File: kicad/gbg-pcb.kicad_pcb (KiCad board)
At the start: 2 copper layers, 99.1 x 99.1 mm, 74 parts, among them J1 1017514, J2 Screw_Terminal_01x04, J3 Screw_Terminal_01x03, J4 1017514, J5 VP0265840000G, J6 Conn_01x09_Pin, J7 Conn_01x02, Q1 SQD40031EL_GE3, Q2 SQD40031EL_GE3, Q3 SQD40031EL_GE3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

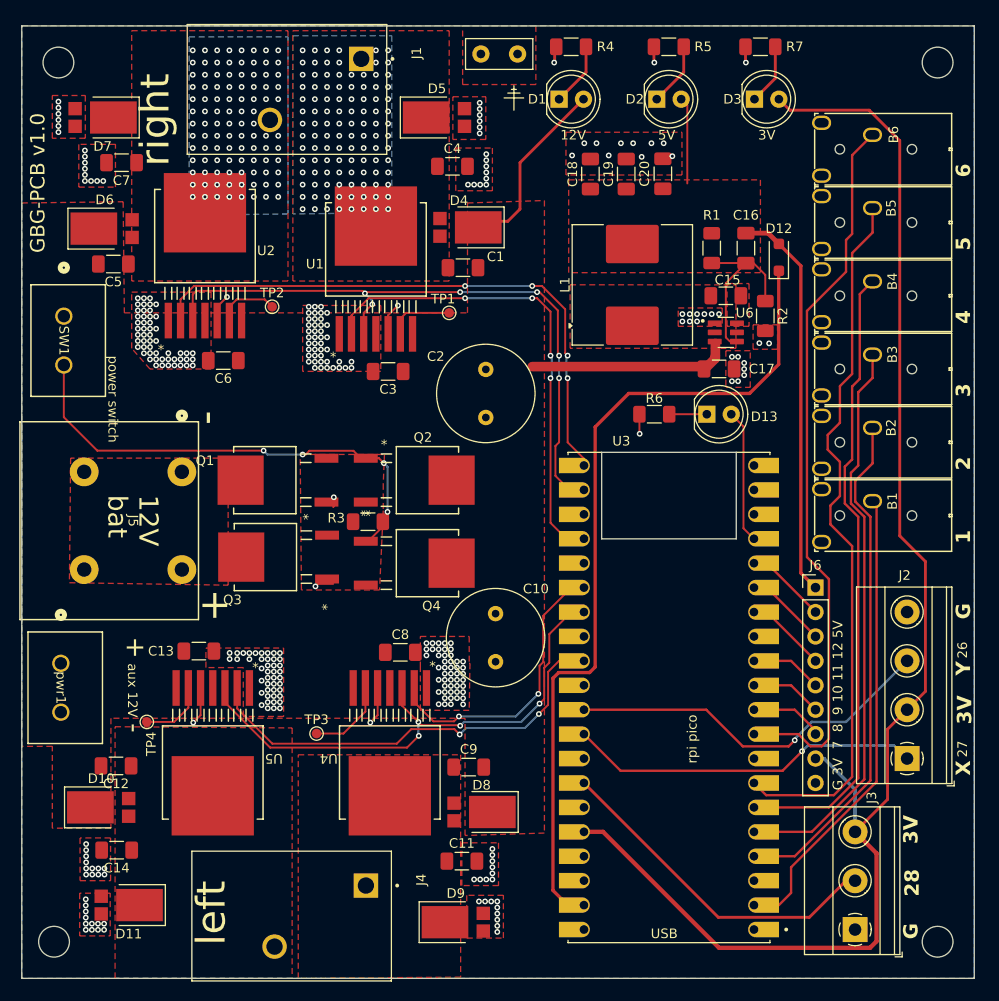
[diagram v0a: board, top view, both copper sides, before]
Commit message: automatically render images
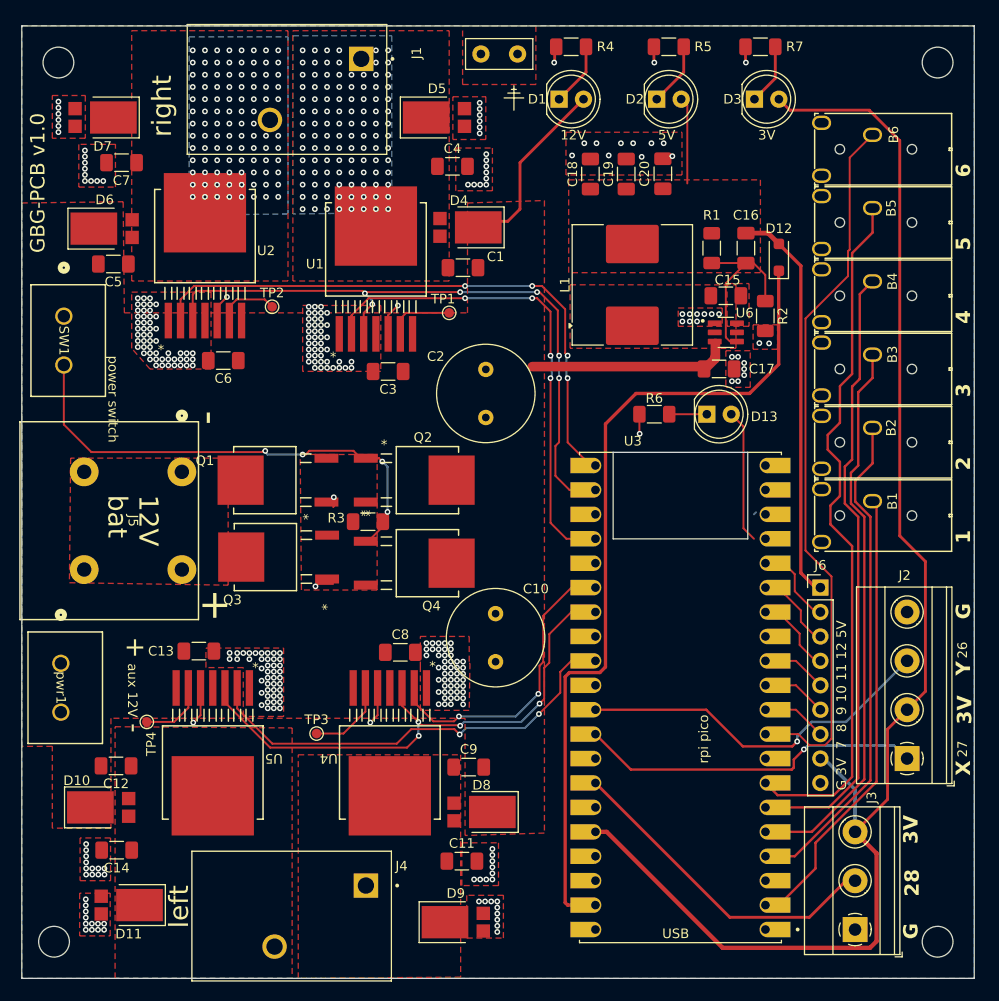
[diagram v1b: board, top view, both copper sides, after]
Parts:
- moved U3 1.19 mm to (108.3, 118.0)
- moved J6 0.51 mm to (122.8, 106.6)
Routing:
- net Net-(D12-K): track 87.3 -> 85.8 mm
- net bt5: track 74.5 -> 73.3 mm
- net +3.3V: track 148.2 -> 147.1 mm
- net left_en: track 55.7 -> 56.9 mm
- net bt4: track 65.5 -> 64.4 mm
- net bt3: track 59.4 -> 58.2 mm
- net bt2: track 53.5 -> 52.3 mm
- net Net-(J3-Pin_2): track 35.6 -> 34.4 mm
- net bt1: track 49.4 -> 48.2 mm
- net Net-(J2-Pin_3): track 38.9 -> 38.0 mm
- net Net-(J6-Pin_7): track 7.68 -> 6.77 mm
- net Net-(J2-Pin_1): track 36.8 -> 36.0 mm
- net bt6: track 75.2 -> 74.5 mm
- net Net-(J6-Pin_6): track 7.45 -> 6.77 mm
- net Net-(J6-Pin_5): track 7.45 -> 6.77 mm
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
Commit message: clean up fil zones
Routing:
- net Net-(D8-A): vias 0 -> 98
- net Net-(D10-A): vias 0 -> 105
- added copper zone on B.Cu, net Net-(D10-A)
- added copper zone on B.Cu, net Net-(D8-A)

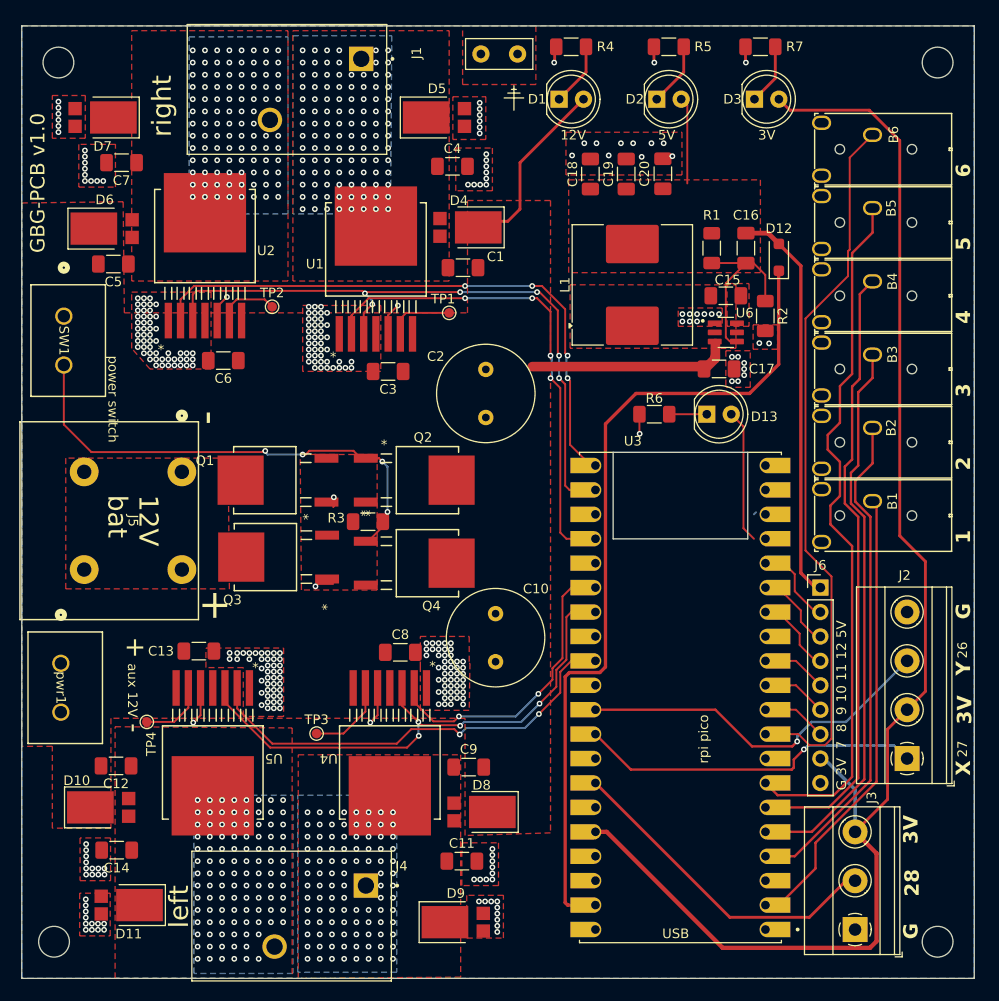
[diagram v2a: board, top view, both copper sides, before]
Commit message: change inductor
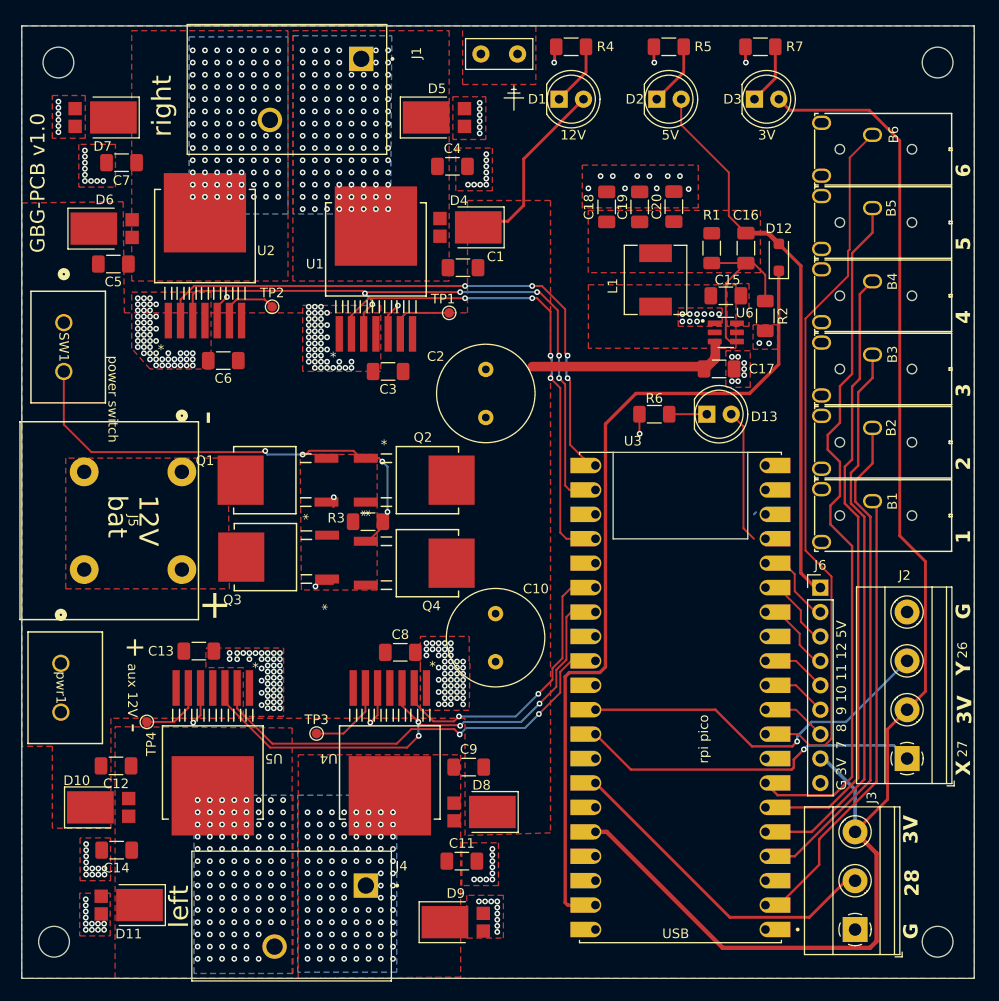
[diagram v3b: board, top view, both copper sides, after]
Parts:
- C15: value 22uF -> 100nF
- C17: value 22uF -> 15uF
- L1: footprint Inductor_SMD:L_Coilcraft_MSS1260T-XXX -> kicad libraries:IND_SRP6540-150M
- moved C18 3.82 mm to (100.6, 67.0)
- moved C19 3.69 mm to (104.0, 67.0)
- moved C20 3.60 mm to (107.6, 66.9)
- moved L1 2.47 mm to (105.7, 74.5)
- moved SW1 0.67 mm to (44.1, 79.0)
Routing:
- net 5V: track 50.2 -> 57.9 mm
- net Net-(U6-SW): track 2.07 -> 0.00 mm
- net Net-(Q2-G): track 51.0 -> 50.3 mm
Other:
- board text added: "sd card? maybe on the back? flyback diodes? could smaller ones be used? think about the +BATT fill - make it thicker? add more capacitors between it and ground? for buck converter, re-do layout. look at datasheet's layout example change motor power screw terminals? think about thermal resistance of parts - how much current can they actually handle? think about how to add heat sinks to this board 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"
- board text removed: "sd card? maybe on the back? flyback diodes? could smaller ones be used? think about the +BATT fill - make it thicker? add more capacitors between it and ground? for buck converter, look at datasheet's layout example change main power screw terminal? it used to be 1017503, consider the same as the motors have 1017514 or terminals with more vertical wire entry 1017514 (screws) or 1017521 (screwless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"

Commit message: move silkscreen
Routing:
- net GND: vias 300 -> 296

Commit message: label pico pins
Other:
- board text added: "15 14 GND 13 led 12 11 10 GND 9 8 7 6 B6 GND 5 B5 4 B4 3 B3 2 B2 GND 1 B1 0"
- board text added: "R2 16 Ren 17 GND R1 18 19 L1 20 Len 21 GND L2 22 RUN Y 26 X 27 GND A2 28 VREF 3.3V EN GND VSYS VBUS"
- board text added: "sd card? maybe on the back? flyback diodes? could smaller ones be used? think about the +BATT fill - make it thicker? add more capacitors between it and ground? for buck converter, redo layout? look at datasheet's layout example change motor power screw terminals? think about thermal resistance of parts - how much current can they actually handle? think about how to add heat sinks to this board c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"
- board text removed: "sd card? maybe on the back? flyback diodes? could smaller ones be used? think about the +BATT fill - make it thicker? add more capacitors between it and ground? for buck converter, re-do layout. look at datasheet's layout example change motor power screw terminals? think about thermal resistance of parts - how much current can they actually handle? think about how to add heat sinks to this board 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"
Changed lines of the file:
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@@
 		(tags "resistor handsolder")
 		(property "Reference" "R6"
-			(at 0 1.651 180)
+			(at 0 -1.614 180)
 			(layer "F.SilkS")
 			(effects
@@
 		(at 108.2548 117.983 180)
 		(property "Reference" "U3"
-			(at 4.953 26.67 0)
+			(at 8.5038 -26.65 0)
 			(layer "F.SilkS")
 			(effects
@@
 		)
 		(fp_line
-			(start 7 25.5)
-			(end -7 25.5)
-			(stroke
-				(width 0.01)
-				(type solid)
-			)
-			(layer "Edge.Cuts")
-		)
-		(fp_line
-			(start 7 16.5)
-			(end 7 25.5)
-			(stroke
-				(width 0.01)
-				(type solid)
-			)
-			(layer "Edge.Cuts")
-		)
-		(fp_line
-			(start -7 25.5)
-			(end -7 16.5)
-			(stroke
-				(width 0.01)
-				(type solid)
-			)
-			(layer "Edge.Cuts")
-		)
-		(fp_line
-			(start -7 16.5)
-			(end 7 16.5)
-			(stroke
-				(width 0.01)
-				(type solid)
-			)
-			(layer "Edge.Cuts")
-		)
-		(fp_line
 			(start 11.54 25.75)
 			(end 11.54 -27.05)
@@
 		)
 		(fp_line
-			(start 7 25.5)
-			(end 7 16.5)
-			(stroke
-				(width 0.127)
-				(type solid)
-			)
-			(layer "F.Fab")
-		)
-		(fp_line
-			(start 7 16.5)
-			(end -7 16.5)
-			(stroke
-				(width 0.127)
-				(type solid)
-			)
-			(layer "F.Fab")
-		)
-		(fp_line
 			(start 4 -25.5)
 			(end 10.5 -25.5)
@@
 		)
 		(fp_line
-			(start -7 16.5)
-			(end -7 25.5)
-			(stroke
-				(width 0.127)
-				(type solid)
-			)
-			(layer "F.Fab")
-		)
-		(fp_line
 			(start -10.5 25.5)
 			(end -10.5 -25.5)
@@
 			)
 		)
+		(zone
+			(net 0)
+			(net_name "")
+			(layers "F.Cu" "B.Cu")
+			(hatch edge 0.5)
+			(connect_pads
+				(clearance 0)
+			)
+			(min_thickness 0.25)
+			(filled_areas_thickness no)
+			(keepout
+				(tracks not_allowed)
+				(vias not_allowed)
+				(pads not_allowed)
+				(copperpour not_allowed)
+				(footprints allowed)
+			)
+			(placement
+				(enabled no)
+				(sheetname "")
+			)
+			(fill
+				(thermal_gap 0.5)
+				(thermal_bridge_width 0.5)
+			)
+			(polygon
+				(pts
+					(xy 115.2548 101.483) (xy 101.2548 101.483) (xy 101.2548 92.483) (xy 115.2548 92.483)
+				)
+			)
+		)
 		(embedded_fonts no)
 		(model "${KIPRJMOD}/kicad libraries/SC0918.step"
@@
 		(tags "LED")
 		(property "Reference" "D13"
-			(at 5.969 0.254 0)
+			(at 5.753 0.114 0)
 			(layer "F.SilkS")
 			(effects
@@
 	)
 	(gr_text "github.com/gobabygocarswithjoysticks/gbg-pcb"
-		(at 104.521 102.362 90)
+		(at 104.751 71.633 0)
+		(layer "B.SilkS")
+		(effects
+			(font
+				(size 1.5 1.5)
+				(thickness 0.2)
+				(bold yes)
+			)
+			(justify left bottom mirror)
+		)
+	)
+	(gr_text "G 3V  7  8  9 10 11 12 5V"
+		(at 124.251 127.633 -90)
 		(layer "B.SilkS")
 		(effects
 			(font
-				(size 1.125 1.125)
+				(size 1.02 1.02)
 				(thickness 0.15)
 			)
@@
 		)
 	)
+	(gr_text "R2 16\nRen 17\nGND\nR1 18\n19\nL1 20\nLen 21\nGND\nL2 22\nRUN\nY 26\nX 27\nGND\nA2 28\nVREF\n3.3V\nEN\nGND\nVSYS\nVBUS"
+		(at 100.251 143.133 0)
+		(layer "B.SilkS")
+		(effects
+			(font
+				(size 1.59 1.5)
+				(thickness 0.2)
+			)
+			(justify right bottom mirror)
+		)
+	)
 	(gr_text "gobabygocarswithjoysticks@gmail.com"
-		(at 108.966 102.362 90)
+		(at 104.751 74.133 0)
 		(layer "B.SilkS")
 		(effects
 			(font
-				(size 1.25 1.25)
-				(thickness 0.15)
+				(size 1.5 1.5)
+				(thickness 0.2)
+			)
+			(justify left bottom mirror)
+		)
+	)
+	(gr_text "15\n14\nGND\n13 led\n12\n11\n10\nGND\n9\n8\n7\n6 B6\nGND\n5 B5\n4 B4\n3 B3\n2 B2\nGND\n1 B1\n0"
+		(at 116.251 143.133 0)
+		(layer "B.SilkS")
+		(effects
+			(font
+				(size 1.59 1.5)
+				(thickness 0.2)
 			)
 			(justify left bottom mirror)
 		)
 	)
-	(gr_text "\nsd card? maybe on the back?\n\nflyback diodes? could smaller ones be used?\n\nthink about the +BATT fill - make it thicker? add more capacitors between it and ground?\n\nfor buck converter, re-do layout. look at datasheet's layout example\n\nchange motor power screw terminals? \n\nthink about thermal resistance of parts - how much current can they actually handle?\n\nthink about how to add heat sinks to this board\n\ncheck values of all components\n\nsilkscreen - labels, add component values?, label pico pins on the back, clean up\n\ntraces - clean up\n\ncheck BOM\n"
+	(gr_text "\nsd card? maybe on the back?\n\nflyback diodes? could smaller ones be used?\n\nthink about the +BATT fill - make it thicker? add more capacitors between it and ground?\n\nfor buck converter, redo layout? look at datasheet's layout example\n\nchange motor power screw terminals? \n\nthink about thermal resistance of parts - how much current can they actually handle?\n\nthink about how to add heat sinks to this board\n\ncheck values of all components\n\nsilkscreen - labels, add component values?, clean up\n\ntraces - clean up\n\ncheck BOM\n"
 		(at 154.432 120.142 0)
 		(layer "User.1")
